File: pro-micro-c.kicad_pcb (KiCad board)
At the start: 2 copper layers, 24 parts, among them J1 USB_C_Receptacle, U1 ProMicro, U2 MIC5219-3.3YM5, U3 ATmega32U4-MU, Y1 Crystal

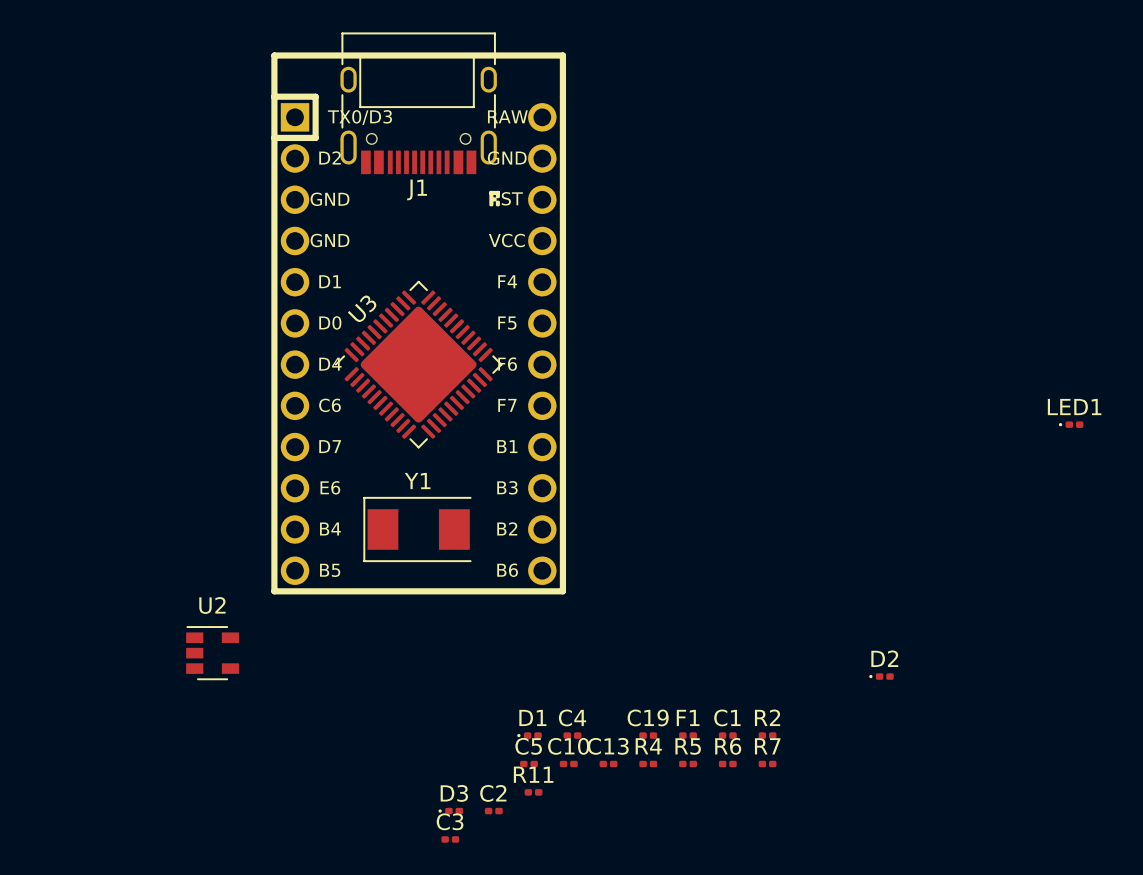
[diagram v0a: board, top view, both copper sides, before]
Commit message: full layout. Doesn't route yet
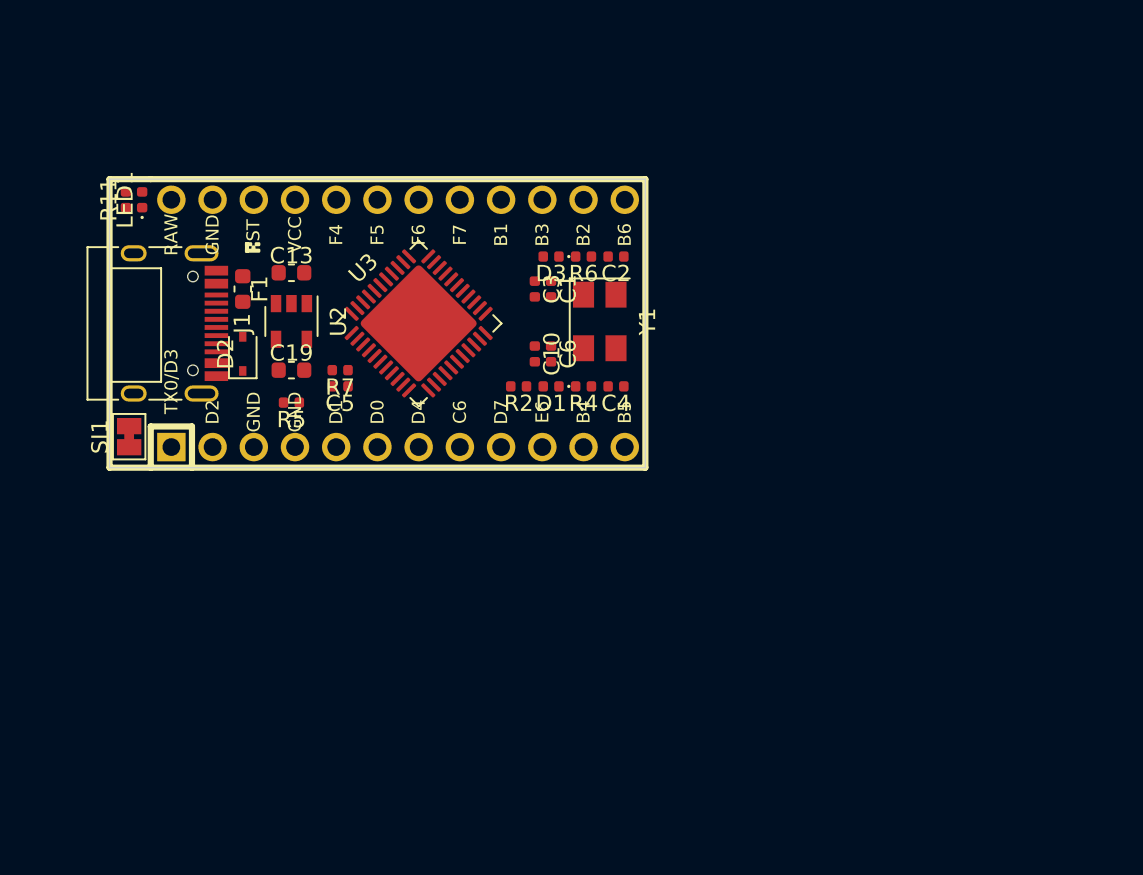
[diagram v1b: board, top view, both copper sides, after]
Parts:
- added C6: 1uF, Capacitor_SMD:C_0402_1005Metric, F.Cu at (125.0, 73.0)
- added SJ1: SolderJumper_2_Bridged, Jumper:SolderJumper-2_P1.3mm_Bridged_Pad1.0x1.5mm, F.Cu at (99.0, 78.1)
- C1, C10, C2, C3, C4, C5: footprint Capacitor_SMD:C_0201_0603Metric -> Capacitor_SMD:C_0402_1005Metric
- C13, C19: footprint Capacitor_SMD:C_0201_0603Metric -> Capacitor_SMD:C_0603_1608Metric
- D1, D3, LED1: footprint LED_SMD:LED_0201_0603Metric -> LED_SMD:LED_0402_1005Metric
- D2: footprint Diode_SMD:D_0201_0603Metric -> Diode_SMD:D_SOD-323
- F1: footprint Fuse:Fuse_0201_0603Metric -> Fuse:Fuse_0603_1608Metric
- R11, R2, R4, R5, R6, R7: footprint Resistor_SMD:R_0201_0603Metric -> Resistor_SMD:R_0402_1005Metric
- Y1: footprint Crystal:Crystal_SMD_0603-2Pin_6.0x3.5mm -> Crystal:Crystal_SMD_5032-4Pin_5.0x3.2mm
- moved LED1 59.1 mm to (99.8, 63.5), turned to 90 degrees
- moved R11 44.3 mm to (98.8, 63.5), turned to 90 degrees
- moved D2 44.3 mm to (106.0, 73.0), turned to 90 degrees
- moved F1 38.9 mm to (106.0, 69.0), turned to 270 degrees
- moved C13 36.0 mm to (109.0, 68.0)
- moved R7 35.8 mm to (112.0, 74.0), turned to 180 degrees
- moved C2 35.0 mm to (129.0, 67.0), turned to 180 degrees
- moved D3 34.7 mm to (125.0, 67.0), turned to 180 degrees
- moved C3 34.3 mm to (124.0, 69.0), turned to 270 degrees
- moved R5 33.1 mm to (109.0, 76.0), turned to 180 degrees
- moved R6 32.5 mm to (127.0, 67.0), turned to 180 degrees
- moved C19 31.5 mm to (109.0, 74.0)
- moved C1 29.6 mm to (125.0, 69.0), turned to 270 degrees
- moved R2 26.4 mm to (123.0, 75.0), turned to 180 degrees
- moved C5 26.0 mm to (112.0, 75.0), turned to 180 degrees
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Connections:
- J1 pad B6: Net-(J1-PadB6) -> Net-(J1-PadA6)
- J1 pad B7: Net-(J1-PadB7) -> Net-(J1-PadA7)
- R7 pad 2: Net-(J1-PadB6) -> Net-(J1-PadA6)
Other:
- board outline added: 33 x 17.8 mm

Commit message: Still doesn't route
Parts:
- C13, C19: footprint Capacitor_SMD:C_0603_1608Metric -> Capacitor_Tantalum_SMD:CP_EIA-3216-10_Kemet-I
- D2: footprint Diode_SMD:D_SOD-323 -> Diode_SMD:D_SOD-123
- F1: footprint Fuse:Fuse_0603_1608Metric -> Fuse:Fuse_1206_3216Metric
- moved R2 19.0 mm to (104.0, 75.0), turned to 270 degrees
- moved C3 18.1 mm to (106.0, 67.0)
- moved LED1 13.1 mm to (106.0, 75.0)
- moved R11 13.1 mm to (105.0, 75.0), turned to 270 degrees
- moved C1 12.2 mm to (113.0, 67.0), turned to 90 degrees
- moved R5 10.3 mm to (104.0, 67.0), turned to 270 degrees
- moved R7 9.90 mm to (105.0, 67.0), turned to 270 degrees
- moved C2 7.81 mm to (123.0, 72.0), turned to 270 degrees
- moved C4 7.81 mm to (123.0, 70.0), turned to 270 degrees
- moved C10 6.08 mm to (123.0, 67.0), turned to 0 degrees
- moved J1 3.33 mm to (97.0, 71.1)
- moved D2 3.20 mm to (103.5, 71.0), turned to 270 degrees
- moved C6 2.83 mm to (123.0, 75.0), turned to 180 degrees
- moved F1 2.00 mm to (105.9, 71.0)
- moved Y1 2.00 mm to (126.0, 71.0)
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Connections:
- C3 pad 1: VCC -> GND
- C3 pad 2: GND -> VCC
- Y1 pad 1: Net-(C2-Pad1) -> Net-(C4-Pad1)
- Y1 pad 2: Net-(C4-Pad1) -> Net-(C2-Pad1)
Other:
- board size 33 x 17.8 mm -> 36.8 x 17.8 mm

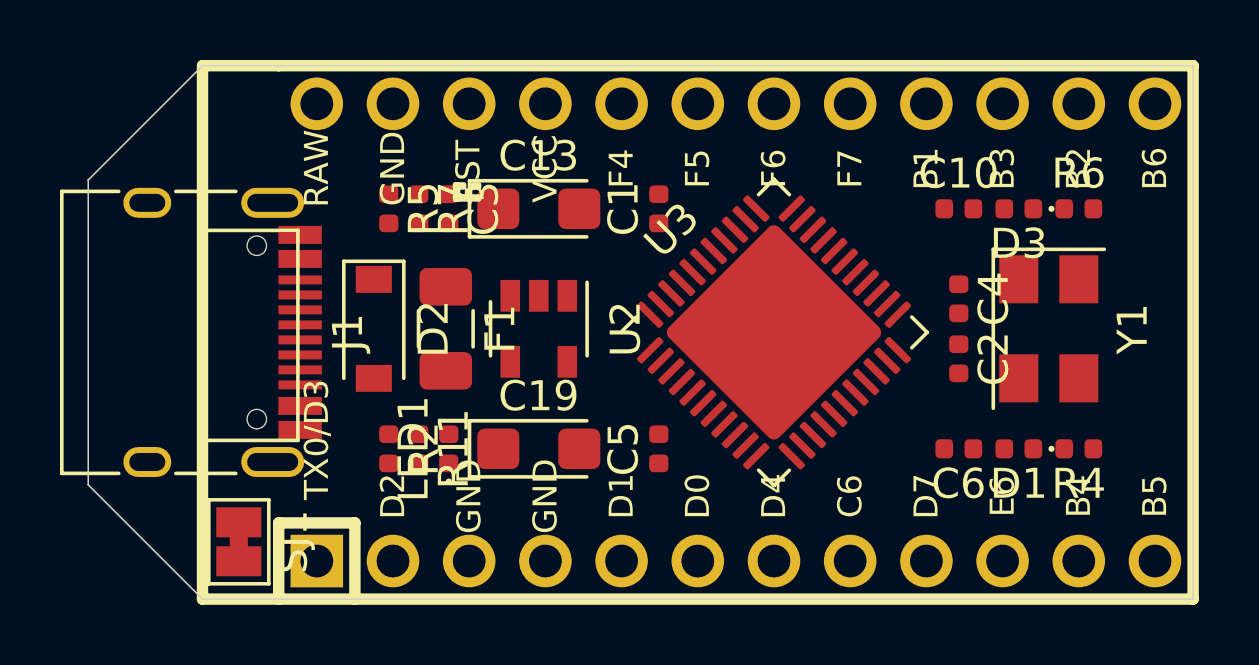
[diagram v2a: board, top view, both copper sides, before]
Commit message: more layout improvements. still doesn't route
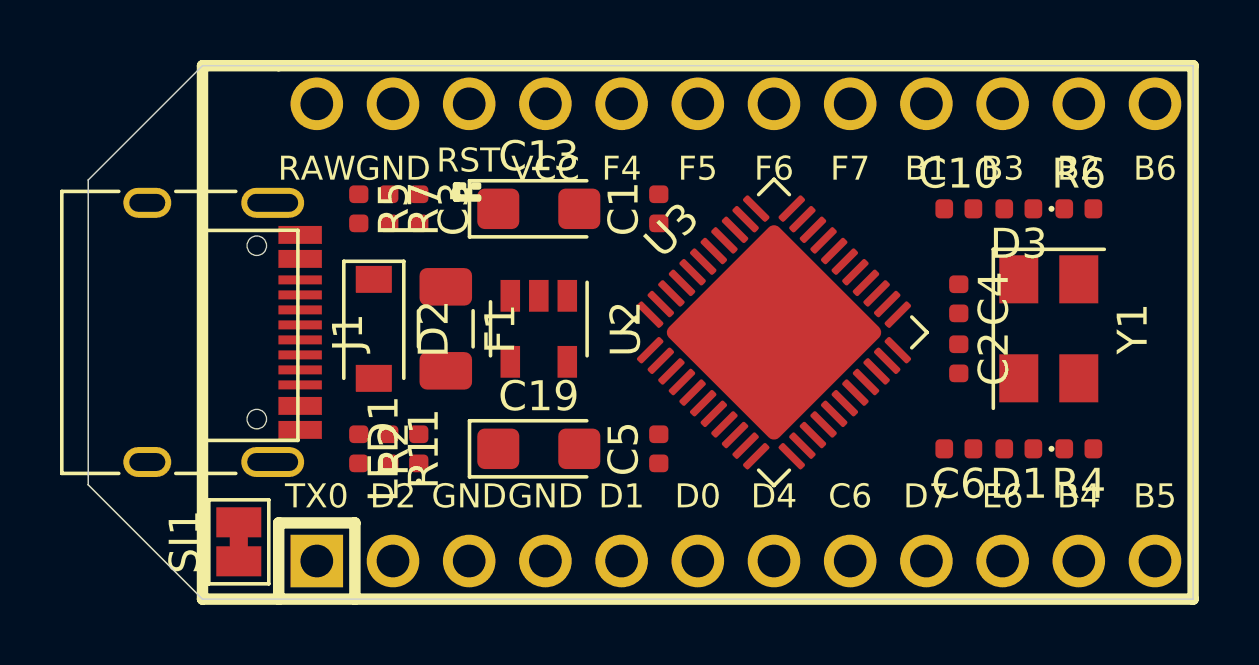
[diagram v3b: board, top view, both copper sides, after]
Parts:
- moved C3 1.00 mm to (105.0, 67.0)
- moved LED1 1.00 mm to (105.0, 75.0)
- moved R11 1.00 mm to (104.0, 75.0)
- moved R2 1.00 mm to (103.0, 75.0)
- moved R5 1.00 mm to (103.0, 67.0)
- moved R7 1.00 mm to (104.0, 67.0)
- turned SJ1 to 90 degrees
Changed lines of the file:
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@@
   (page A4)
   (layers
-    (0 F.Cu signal hide)
-    (31 B.Cu signal hide)
-    (32 B.Adhes user hide)
-    (33 F.Adhes user hide)
-    (34 B.Paste user hide)
+    (0 F.Cu signal)
+    (31 B.Cu signal)
+    (32 B.Adhes user)
+    (33 F.Adhes user)
+    (34 B.Paste user)
     (35 F.Paste user)
     (36 B.SilkS user)
-    (37 F.SilkS user hide)
+    (37 F.SilkS user)
     (38 B.Mask user)
-    (39 F.Mask user hide)
+    (39 F.Mask user)
     (40 Dwgs.User user)
     (41 Cmts.User user)
@@
   )
   (module Resistor_SMD:R_0402_1005Metric (layer F.Cu)
-    (at 105 75 270)
+    (at 104 75 270)
     (descr "Resistor SMD 0402 (1005 Metric), square (rectangular) end terminal, IPC_7351 nominal, (Body size source: http://www.tortai-tech.com/upload/download/2011102023233369053.pdf), generated with kicad-footprint-generator")
     (tags resistor)
@@
   )
   (module Resistor_SMD:R_0402_1005Metric (layer F.Cu)
-    (at 105 67 270)
+    (at 104 67 270)
     (descr "Resistor SMD 0402 (1005 Metric), square (rectangular) end terminal, IPC_7351 nominal, (Body size source: http://www.tortai-tech.com/upload/download/2011102023233369053.pdf), generated with kicad-footprint-generator")
     (tags resistor)
@@
   )
   (module Resistor_SMD:R_0402_1005Metric (layer F.Cu)
-    (at 104 67 270)
+    (at 103 67 270)
     (descr "Resistor SMD 0402 (1005 Metric), square (rectangular) end terminal, IPC_7351 nominal, (Body size source: http://www.tortai-tech.com/upload/download/2011102023233369053.pdf), generated with kicad-footprint-generator")
     (tags resistor)
@@
   )
   (module Resistor_SMD:R_0402_1005Metric (layer F.Cu)
-    (at 104 75 270)
+    (at 103 75 270)
     (descr "Resistor SMD 0402 (1005 Metric), square (rectangular) end terminal, IPC_7351 nominal, (Body size source: http://www.tortai-tech.com/upload/download/2011102023233369053.pdf), generated with kicad-footprint-generator")
     (tags resistor)
@@
   )
   (module LED_SMD:LED_0402_1005Metric (layer F.Cu)
-    (at 106 75 90)
+    (at 105 75 90)
     (descr "LED SMD 0402 (1005 Metric), square (rectangular) end terminal, IPC_7351 nominal, (Body size source: http://www.tortai-tech.com/upload/download/2011102023233369053.pdf), generated with kicad-footprint-generator")
     (tags LED)
@@
   )
   (module Capacitor_SMD:C_0402_1005Metric (layer F.Cu)
-    (at 106 67 270)
+    (at 105 67 270)
     (descr "Capacitor SMD 0402 (1005 Metric), square (rectangular) end terminal, IPC_7351 nominal, (Body size source: http://www.tortai-tech.com/upload/download/2011102023233369053.pdf), generated with kicad-footprint-generator")
     (tags capacitor)
@@
   )
   (module Jumper:SolderJumper-2_P1.3mm_Bridged_Pad1.0x1.5mm (layer F.Cu)
-    (at 99 78.1 270)
+    (at 99 78.1 90)
     (descr "SMD Solder Jumper, 1x1.5mm Pads, 0.3mm gap, bridged with 1 copper strip")
     (tags "solder jumper open")
@@
     (fp_line (start 1.4 1) (end -1.4 1) (layer F.SilkS) (width 0.12))
     (fp_line (start -1.4 1) (end -1.4 -1) (layer F.SilkS) (width 0.12))
-    (pad 2 smd rect (at 0.65 0 270) (size 1 1.5) (layers F.Cu F.Mask)
+    (pad 2 smd rect (at 0.65 0 90) (size 1 1.5) (layers F.Cu F.Mask)
       (net 4 VCC))
-    (pad 1 smd rect (at -0.65 0 270) (size 1 1.5) (layers F.Cu F.Mask)
+    (pad 1 smd rect (at -0.65 0 90) (size 1 1.5) (layers F.Cu F.Mask)
       (net 9 "Net-(D2-Pad2)"))
   )
@@
     (fp_line (start 15.24 8.89) (end 15.24 -8.89) (layer F.SilkS) (width 0.381))
     (fp_line (start -15.24 8.89) (end 15.24 8.89) (layer F.SilkS) (width 0.381))
-    (fp_text user TX0/D3 (at -13.97 3.571872 -270) (layer F.SilkS)
+    (fp_text user TX0 (at -13.97 5.461 -180) (layer F.SilkS)
       (effects (font (size 0.8 0.8) (thickness 0.15)))
     )
@@
       (effects (font (size 0.8 0.8) (thickness 0.15)) (justify mirror))
     )
-    (fp_text user D2 (at -11.43 5.461 -270) (layer F.SilkS)
-      (effects (font (size 0.8 0.8) (thickness 0.15)))
-    )
-    (fp_text user D0 (at -1.27 5.461 -270) (layer F.SilkS)
-      (effects (font (size 0.8 0.8) (thickness 0.15)))
-    )
-    (fp_text user D1 (at -3.81 5.461 -270) (layer F.SilkS)
-      (effects (font (size 0.8 0.8) (thickness 0.15)))
-    )
-    (fp_text user GND (at -6.35 5.461 -270) (layer F.SilkS)
-      (effects (font (size 0.8 0.8) (thickness 0.15)))
-    )
-    (fp_text user GND (at -8.89 5.461 -270) (layer F.SilkS)
-      (effects (font (size 0.8 0.8) (thickness 0.15)))
-    )
-    (fp_text user D4 (at 1.27 5.461 -270) (layer F.SilkS)
-      (effects (font (size 0.8 0.8) (thickness 0.15)))
-    )
-    (fp_text user C6 (at 3.81 5.461 -270) (layer F.SilkS)
-      (effects (font (size 0.8 0.8) (thickness 0.15)))
-    )
-    (fp_text user D7 (at 6.35 5.461 -270) (layer F.SilkS)
-      (effects (font (size 0.8 0.8) (thickness 0.15)))
-    )
-    (fp_text user E6 (at 8.89 5.461 -270) (layer F.SilkS)
-      (effects (font (size 0.8 0.8) (thickness 0.15)))
-    )
-    (fp_text user B4 (at 11.43 5.461 -270) (layer F.SilkS)
-      (effects (font (size 0.8 0.8) (thickness 0.15)))
-    )
-    (fp_text user B5 (at 13.97 5.461 -270) (layer F.SilkS)
-      (effects (font (size 0.8 0.8) (thickness 0.15)))
-    )
-    (fp_text user B6 (at 13.97 -5.461 -270) (layer F.SilkS)
+    (fp_text user D2 (at -11.43 5.461 -180) (layer F.SilkS)
+      (effects (font (size 0.8 0.8) (thickness 0.15)))
+    )
+    (fp_text user D0 (at -1.27 5.461 -180) (layer F.SilkS)
+      (effects (font (size 0.8 0.8) (thickness 0.15)))
+    )
+    (fp_text user D1 (at -3.81 5.461 -180) (layer F.SilkS)
+      (effects (font (size 0.8 0.8) (thickness 0.15)))
+    )
+    (fp_text user GND (at -6.35 5.461 -180) (layer F.SilkS)
+      (effects (font (size 0.8 0.8) (thickness 0.15)))
+    )
+    (fp_text user GND (at -8.89 5.461 -180) (layer F.SilkS)
+      (effects (font (size 0.8 0.8) (thickness 0.15)))
+    )
+    (fp_text user D4 (at 1.27 5.461 -180) (layer F.SilkS)
+      (effects (font (size 0.8 0.8) (thickness 0.15)))
+    )
+    (fp_text user C6 (at 3.81 5.461 -180) (layer F.SilkS)
+      (effects (font (size 0.8 0.8) (thickness 0.15)))
+    )
+    (fp_text user D7 (at 6.35 5.461 -180) (layer F.SilkS)
+      (effects (font (size 0.8 0.8) (thickness 0.15)))
+    )
+    (fp_text user E6 (at 8.89 5.461 -180) (layer F.SilkS)
+      (effects (font (size 0.8 0.8) (thickness 0.15)))
+    )
+    (fp_text user B4 (at 11.43 5.461 -180) (layer F.SilkS)
+      (effects (font (size 0.8 0.8) (thickness 0.15)))
+    )
+    (fp_text user B5 (at 13.97 5.461 -180) (layer F.SilkS)
+      (effects (font (size 0.8 0.8) (thickness 0.15)))
+    )
+    (fp_text user B6 (at 13.97 -5.461 -180) (layer F.SilkS)
       (effects (font (size 0.8 0.8) (thickness 0.15)))
     )
@@
       (effects (font (size 0.8 0.8) (thickness 0.15)) (justify mirror))
     )
-    (fp_text user B3 (at 8.89 -5.461 -270) (layer F.SilkS)
-      (effects (font (size 0.8 0.8) (thickness 0.15)))
-    )
-    (fp_text user B1 (at 6.35 -5.461 -270) (layer F.SilkS)
+    (fp_text user B3 (at 8.89 -5.461 -180) (layer F.SilkS)
+      (effects (font (size 0.8 0.8) (thickness 0.15)))
+    )
+    (fp_text user B1 (at 6.35 -5.461 -180) (layer F.SilkS)
       (effects (font (size 0.8 0.8) (thickness 0.15)))
     )
@@
       (effects (font (size 0.8 0.8) (thickness 0.15)) (justify mirror))
     )
-    (fp_text user F4 (at -3.81 -5.461 -270) (layer F.SilkS)
-      (effects (font (size 0.8 0.8) (thickness 0.15)))
-    )
-    (fp_text user VCC (at -6.35 -5.461 -270) (layer F.SilkS)
-      (effects (font (size 0.8 0.8) (thickness 0.15)))
-    )
-    (fp_text user ST (at -8.92 -5.73312 -270) (layer F.SilkS)
-      (effects (font (size 0.8 0.8) (thickness 0.15)))
-    )
-    (fp_text user GND (at -11.43 -5.461 -270) (layer F.SilkS)
-      (effects (font (size 0.8 0.8) (thickness 0.15)))
-    )
-    (fp_text user RAW (at -13.97 -5.461 -270) (layer F.SilkS)
+    (fp_text user F4 (at -3.81 -5.461 -180) (layer F.SilkS)
+      (effects (font (size 0.8 0.8) (thickness 0.15)))
+    )
+    (fp_text user VCC (at -6.35 -5.461 -180) (layer F.SilkS)
+      (effects (font (size 0.8 0.8) (thickness 0.15)))
+    )
+    (fp_text user RST (at -8.92 -5.73312 -180) (layer F.SilkS)
+      (effects (font (size 0.8 0.8) (thickness 0.15)))
+    )
+    (fp_text user GND (at -11.43 -5.461 -180) (layer F.SilkS)
+      (effects (font (size 0.8 0.8) (thickness 0.15)))
+    )
+    (fp_text user RAW (at -13.97 -5.461 -180) (layer F.SilkS)
       (effects (font (size 0.8 0.8) (thickness 0.15)))
     )
@@
       (effects (font (size 0.8 0.8) (thickness 0.15)) (justify mirror))
     )
-    (fp_text user F5 (at -1.27 -5.461 -270) (layer F.SilkS)
-      (effects (font (size 0.8 0.8) (thickness 0.15)))
-    )
-    (fp_text user F6 (at 1.27 -5.461 -270) (layer F.SilkS)
-      (effects (font (size 0.8 0.8) (thickness 0.15)))
-    )
-    (fp_text user F7 (at 3.81 -5.461 -270) (layer F.SilkS)
+    (fp_text user F5 (at -1.27 -5.461 -180) (layer F.SilkS)
+      (effects (font (size 0.8 0.8) (thickness 0.15)))
+    )
+    (fp_text user F6 (at 1.27 -5.461 -180) (layer F.SilkS)
+      (effects (font (size 0.8 0.8) (thickness 0.15)))
+    )
+    (fp_text user F7 (at 3.81 -5.461 -180) (layer F.SilkS)
       (effects (font (size 0.8 0.8) (thickness 0.15)))
     )
@@
       (effects (font (size 0.8 0.8) (thickness 0.15)) (justify mirror))
     )
-    (fp_text user B2 (at 11.43 -5.461 -270) (layer F.SilkS)
-      (effects (font (size 0.8 0.8) (thickness 0.15)))
-    )
+    (fp_text user B2 (at 11.43 -5.461 -180) (layer F.SilkS)
+      (effects (font (size 0.8 0.8) (thickness 0.15)))
+    )

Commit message: Checkpoint. Still doesn't route.
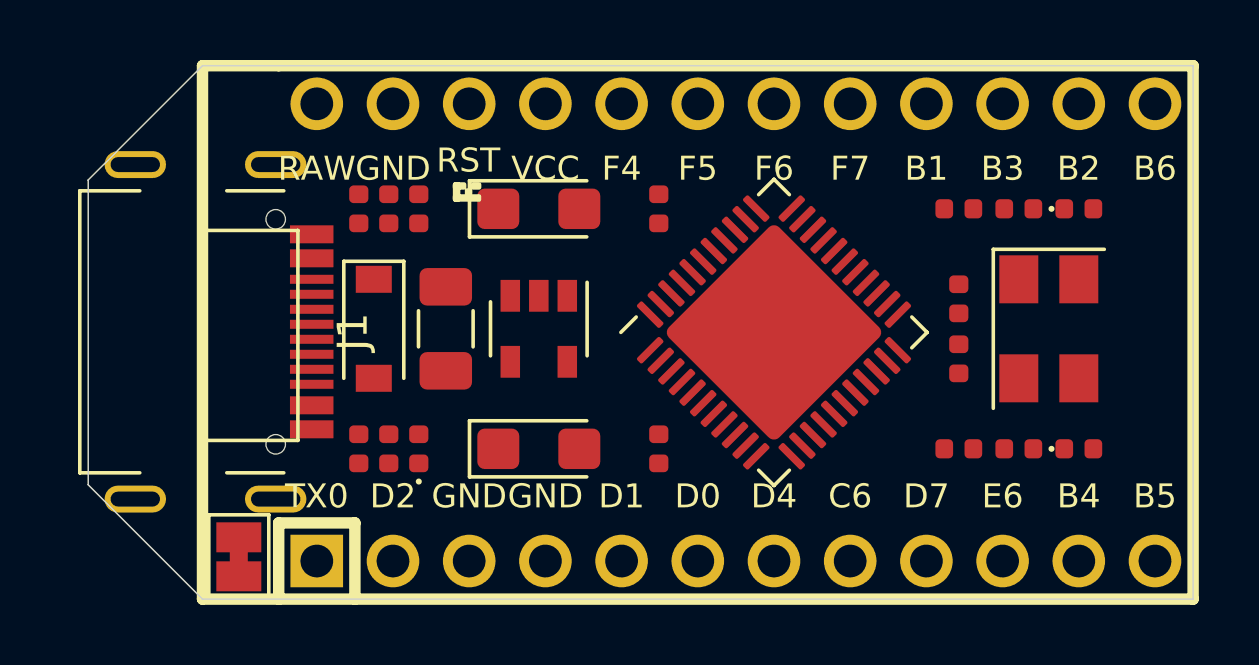
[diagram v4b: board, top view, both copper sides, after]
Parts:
- J1: footprint Connector_USB:USB_C_Receptacle_HRO_TYPE-C-31-M-12 -> keycad:USB_C_Receptacle_HRO_TYPE-C-31-M-14
- moved J1 3.20 mm to (93.8, 71.1)
- moved SJ1 0.50 mm to (99.0, 78.6)
